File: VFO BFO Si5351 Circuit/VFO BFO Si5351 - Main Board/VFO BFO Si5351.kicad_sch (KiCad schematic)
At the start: 33 parts, among them J1 I2C Bus, J10 VIN +12V, J11 GND +5V +9V +12, J12 VFO_Front_Pannel, J2 Band, J3 Mode, J4 AGC, J5 ATT, J6 BFO, J7 TX, J8 IN RTTY, J9 IN S_meter, M1 Si5351A module, U1 ESP32-DEVKITC-32D, U2 PCF8574AP, U3 LM7809, U4 LM7805, U5 24LC32

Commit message: ultimato PCB
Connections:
- no-connect marks 20 -> 19
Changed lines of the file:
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@@
-	)
-	(no_connect
-		(at 88.9 63.5)
 	)
 	(no_connect

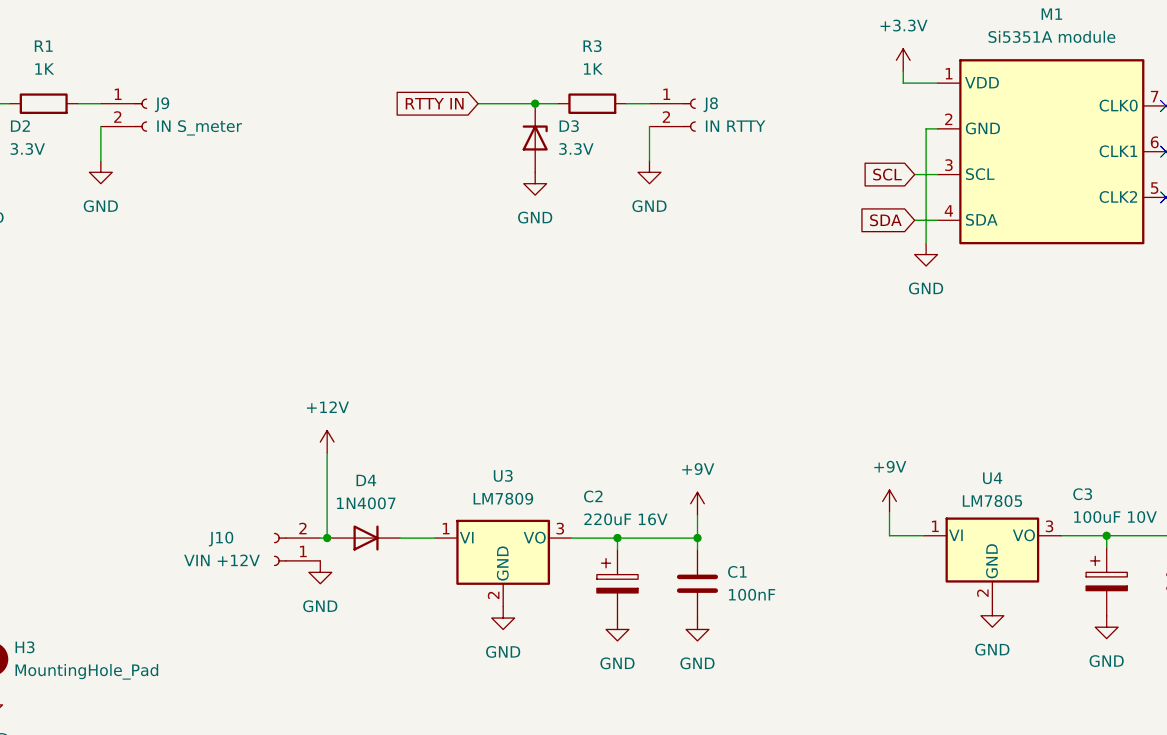
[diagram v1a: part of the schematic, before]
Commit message: Mod code end PCB
Schema elettrico Main-board and Front-panel correzione impronta SI5351 e PCB
Pulizia Codice ed implementazione out digitale  BFO
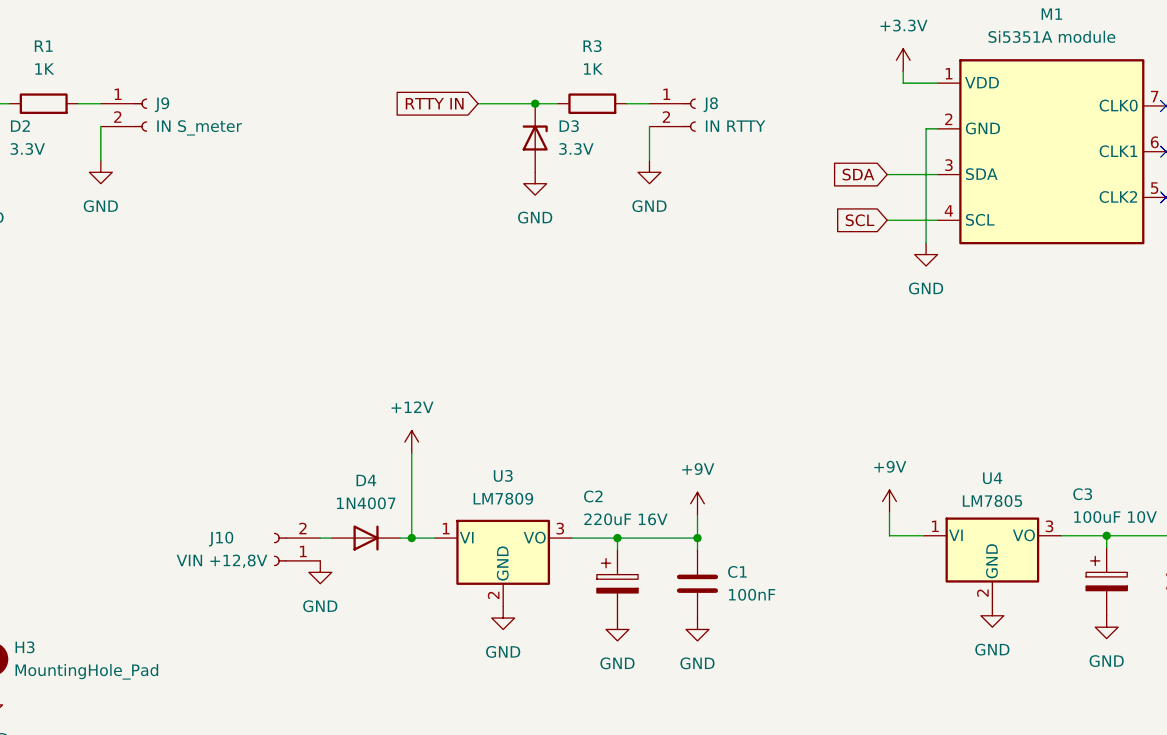
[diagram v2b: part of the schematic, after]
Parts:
- J10: value VIN +12V -> VIN +12,8V
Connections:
- net +12V: now also D4.1 (K), U3.1 (VI); no longer D4.2 (A), J10.2 (Pin_2)
- net SCL: now also M1.4 (SCL); no longer M1.3 (SCL)
- net SDA: now also M1.3 (SDA); no longer M1.4 (SDA)
- new net: D4.2 (A), J10.2 (Pin_2)
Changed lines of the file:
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@@
 	)
 	(junction
-		(at 173.99 144.018)
-		(diameter 0)
-		(color 0 0 0 0)
-	)
-	(junction
 		(at 146.812 49.53)
 		(diameter 0)
@@
 	)
 	(junction
+		(at 183.388 144.018)
+		(diameter 0)
+		(color 0 0 0 0)
+	)
+	(junction
 		(at 156.972 59.69)
 		(diameter 0)
@@
 	(wire
 		(pts
-			(xy 239.268 103.632) (xy 241.808 103.632)
-		)
-		(stroke
-			(width 0)
-			(type default)
-		)
-	)
-	(wire
-		(pts
 			(xy 260.604 143.764) (xy 255.524 143.764)
 		)
@@
 	(wire
 		(pts
+			(xy 236.22 103.632) (xy 241.808 103.632)
+		)
+		(stroke
+			(width 0)
+			(type default)
+		)
+	)
+	(wire
+		(pts
 			(xy 240.03 41.91) (xy 240.03 44.45)
 		)
@@
 	(wire
 		(pts
-			(xy 173.228 144.018) (xy 173.99 144.018)
+			(xy 173.228 144.018) (xy 174.498 144.018)
 		)
 		(stroke
@@
 	(wire
 		(pts
-			(xy 139.192 33.782) (xy 139.192 41.91)
+			(xy 236.22 108.712) (xy 241.808 108.712)
 		)
 		(stroke
@@
 	(wire
 		(pts
-			(xy 207.264 95.758) (xy 209.804 95.758)
+			(xy 183.388 144.018) (xy 182.118 144.018)
 		)
 		(stroke
@@
 	(wire
 		(pts
-			(xy 154.432 57.15) (xy 201.676 57.15)
+			(xy 139.192 33.782) (xy 139.192 41.91)
 		)
 		(stroke
@@
 	(wire
 		(pts
-			(xy 173.99 144.018) (xy 174.498 144.018)
+			(xy 207.264 95.758) (xy 209.804 95.758)
+		)
+		(stroke
+			(width 0)
+			(type default)
+		)
+	)
+	(wire
+		(pts
+			(xy 154.432 57.15) (xy 201.676 57.15)
 		)
 		(stroke
@@
 	(wire
 		(pts
-			(xy 173.99 134.62) (xy 173.99 144.018)
+			(xy 183.388 134.62) (xy 183.388 144.018)
 		)
 		(stroke
@@
 	(wire
 		(pts
-			(xy 185.928 144.018) (xy 182.118 144.018)
+			(xy 185.928 144.018) (xy 183.388 144.018)
 		)
 		(stroke
@@
 	(wire
 		(pts
-			(xy 239.268 108.712) (xy 241.808 108.712)
-		)
-		(stroke
-			(width 0)
-			(type default)
-		)
-	)
-	(wire
-		(pts
 			(xy 110.49 39.37) (xy 110.49 41.91)
 		)
@@
 	(global_label "SDA"
 		(shape input)
-		(at 239.268 108.712 180)
+		(at 236.22 103.632 180)
 		(fields_autoplaced yes)
 		(effects
@@
 		)
 		(property "Intersheetrefs" "${INTERSHEET_REFS}"
-			(at 232.7147 108.712 0)
+			(at 229.6667 103.632 0)
 			(effects
 				(font
@@
 	(global_label "SCL"
 		(shape input)
-		(at 239.268 103.632 180)
+		(at 236.22 108.712 180)
 		(fields_autoplaced yes)
 		(effects
@@
 		)
 		(property "Intersheetrefs" "${INTERSHEET_REFS}"
-			(at 232.7752 103.632 0)
+			(at 229.7272 108.712 0)
 			(effects
 				(font
@@
 	(symbol
 		(lib_id "power:+12V")
-		(at 173.99 134.62 0)
+		(at 183.388 134.62 0)
 		(unit 1)
 		(exclude_from_sim no)
@@
 		(fields_autoplaced yes)
 		(property "Reference" "#PWR045"
-			(at 173.99 138.43 0)
+			(at 183.388 138.43 0)
 			(effects
 				(font
@@
 		)
 		(property "Value" "+12V"
-			(at 173.99 129.54 0)
+			(at 183.388 129.54 0)
 			(effects
 				(font
@@
 		)
 		(property "Footprint" ""
-			(at 173.99 134.62 0)
+			(at 183.388 134.62 0)
 			(effects
 				(font
@@
 		)
 		(property "Datasheet" ""
-			(at 173.99 134.62 0)
+			(at 183.388 134.62 0)
 			(effects
 				(font
@@
 		)
 		(property "Description" "Power symbol creates a global label with name \"+12V\""
-			(at 173.99 134.62 0)
+			(at 183.388 134.62 0)
 			(effects
 				(font
@@
 			)
 		)
-		(property "Value" "VIN +12V"
+		(property "Value" "VIN +12,8V"
 			(at 162.306 146.558 0)
 			(effects
